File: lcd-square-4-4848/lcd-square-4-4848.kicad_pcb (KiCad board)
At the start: 2 copper layers, 77 x 77 mm, 42 parts, among them J1 SWD, J2 Conn_01x40_MountingPin, J4 USB_C_Receptacle_USB2.0_16P, SW1 BOOT0, SW2 RST, U1 siplex-som-s16, U2 TPS61169

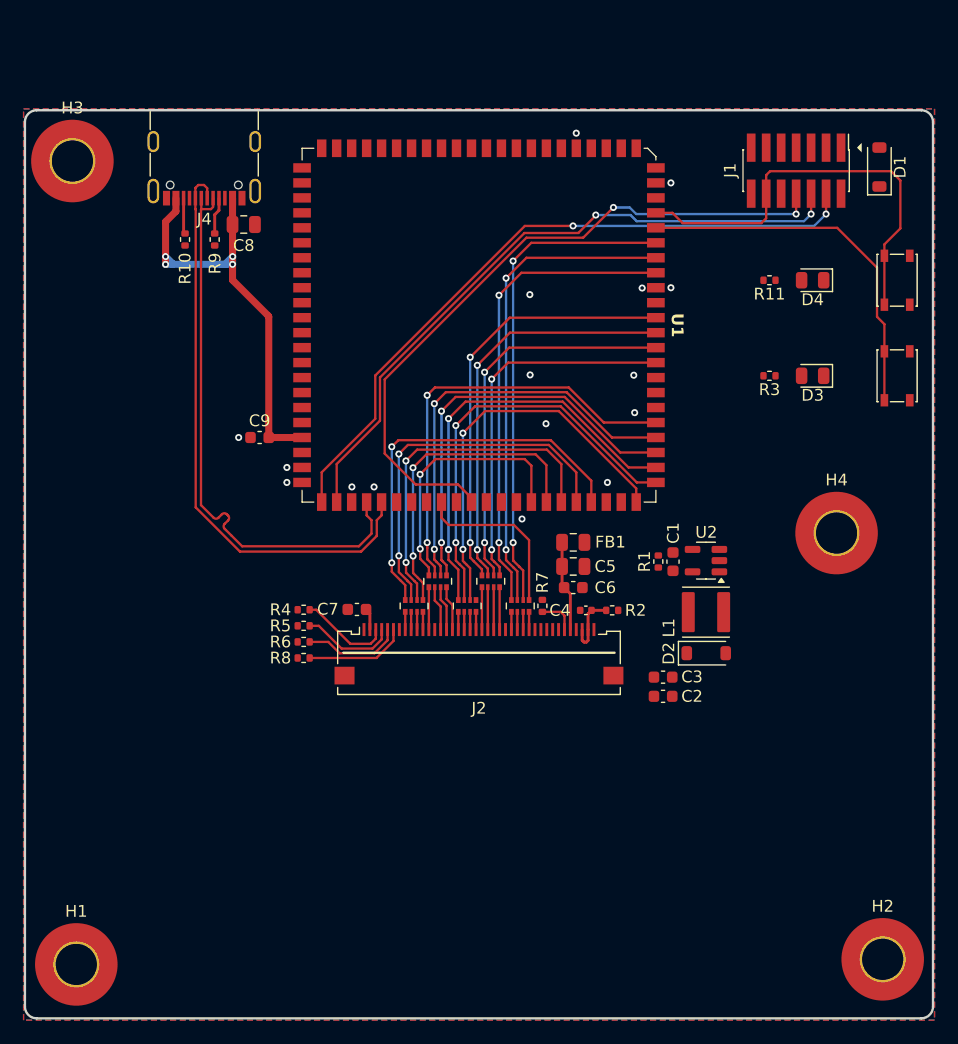
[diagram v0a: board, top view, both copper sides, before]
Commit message: LCD 4inch 480-480 on progress
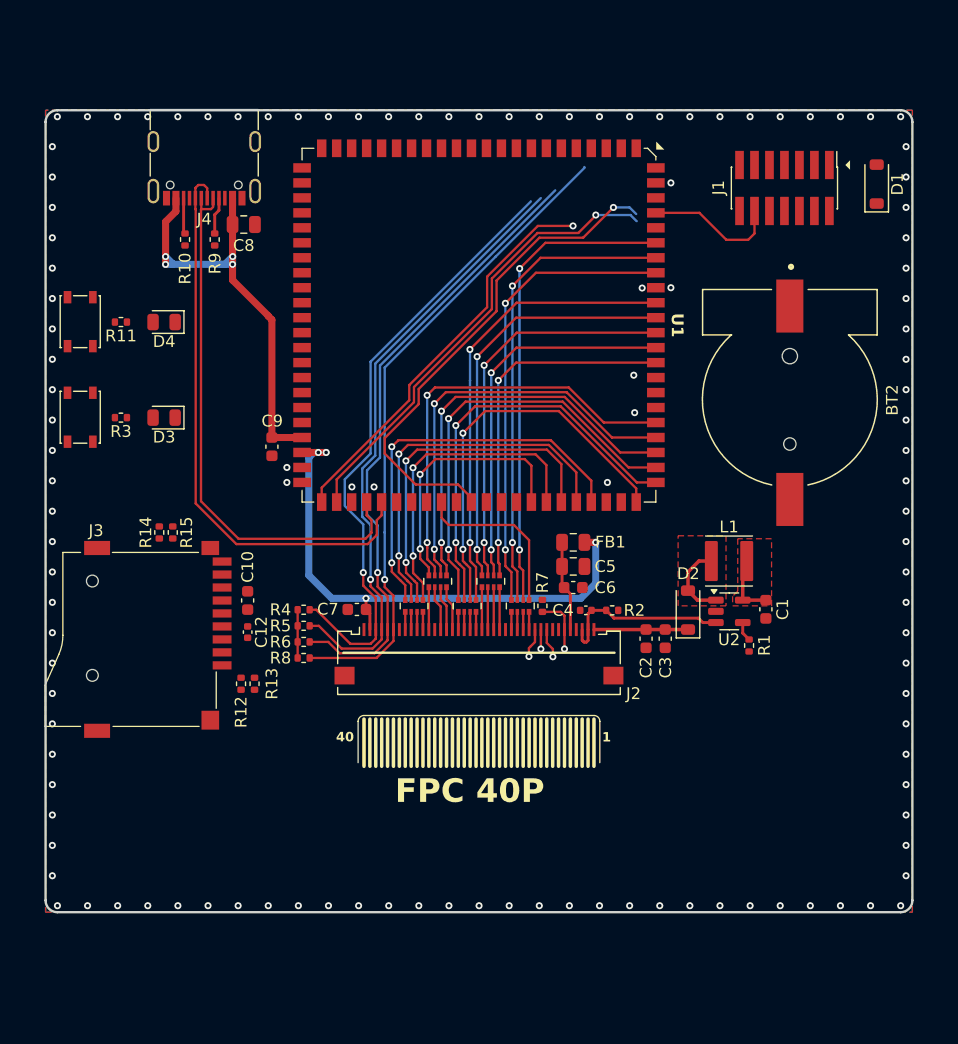
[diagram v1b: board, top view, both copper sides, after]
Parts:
- removed H1, H2, H3, H4: MountingHole_Pad, MountingHole:MountingHole_3.5mm_Pad_TopOnly
- added BT2: S8411-45R, CR1220-Batt-conn-S8411-45R:CR1220-Batt-conn-S8411-45R, F.Cu at (170.9, 83.5)
- added C10: 1u, Capacitor_SMD:C_0603_1608Metric, F.Cu at (124.9, 100.5)
- added C12: 100n, Capacitor_SMD:C_0402_1005Metric, F.Cu at (124.9, 103.1)
- added G***: LOGO, neochrom-logo:neochrom-logo-15, F.Cu at (168.3, 108.8)
- added J3: Micro_SD_Card_Det1, TF-115:SD-TF-115, F.Cu at (117.5, 103.8)
- added R12: 10K, Resistor_SMD:R_0402_1005Metric, F.Cu at (124.4, 107.5)
- added R13: 10K, Resistor_SMD:R_0402_1005Metric, F.Cu at (125.5, 107.5)
- added R14: 10K, Resistor_SMD:R_0402_1005Metric, F.Cu at (117.4, 94.7)
- added R15: 10K, Resistor_SMD:R_0402_1005Metric, F.Cu at (118.6, 94.7)
- moved SW1 69.4 mm to (110.7, 84.9)
- moved SW2 69.4 mm to (110.7, 76.8)
- moved D3 55.1 mm to (117.9, 85.0)
- moved D4 55.1 mm to (117.9, 76.9)
- moved R11 55.1 mm to (114.2, 76.9)
- moved R3 55.1 mm to (114.2, 85.0)
- moved R1 10.5 mm to (167.5, 104.3)
- moved C1 8.85 mm to (168.9, 101.2), turned to -90 degrees
- moved C2 5.10 mm to (158.7, 103.7), turned to -90 degrees
- moved L1 4.75 mm to (165.8, 97.1), turned to 180 degrees
- moved U2 4.74 mm to (165.8, 101.4), turned to 0 degrees
- moved D2 3.97 mm to (162.3, 101.3), turned to 90 degrees
- moved C3 3.27 mm to (160.4, 103.7), turned to -90 degrees
- moved J1 1.77 mm to (170.5, 65.5)
- moved D1 1.46 mm to (178.3, 65.2)
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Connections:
- net Net-(D2-A) renamed /SW
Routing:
- net +3V3: track 1.84 -> 50.7 mm, vias 0 -> 4
- net /LCD_TP_INT: track 8.67 -> 55.2 mm, vias 0 -> 1
- net /LCD_TP_SDA: track 8.36 -> 52.9 mm, vias 0 -> 1
- net /LCD_TP_RST: track 7.75 -> 51.7 mm, vias 0 -> 1
- net /LCD_TP_SCL: track 8.06 -> 51.6 mm, vias 0 -> 1
- net /B7: track 0.00 -> 38.9 mm, vias 0 -> 2
- net /BOOT0: track 31.7 -> 0.00 mm
- net /RESET: track 36.5 -> 11.4 mm
- net /SWDIO: track 58.2 -> 34.0 mm, vias 2 -> 1
- net /SWCLK: track 56.6 -> 39.2 mm, vias 2 -> 1
- net /SWO: track 58.4 -> 42.5 mm, vias 2 -> 1
- net /LED_K: track 5.45 -> 15.2 mm
- net /LED_A: track 0.00 -> 7.98 mm
- net /SW: track 0.00 -> 6.65 mm
- net +5V: track 0.00 -> 5.42 mm
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- added copper zone on F.Cu, net +5V
- added copper zone on F.Cu, net /SW
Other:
- board size 77 x 77 mm -> 73.5 x 68 mm
- board text added: "1"
- board text added: "40"
- board text added: "FPC 40P"
- board text removed: "FPC CONN EDGE"

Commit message: Change SD card orientation
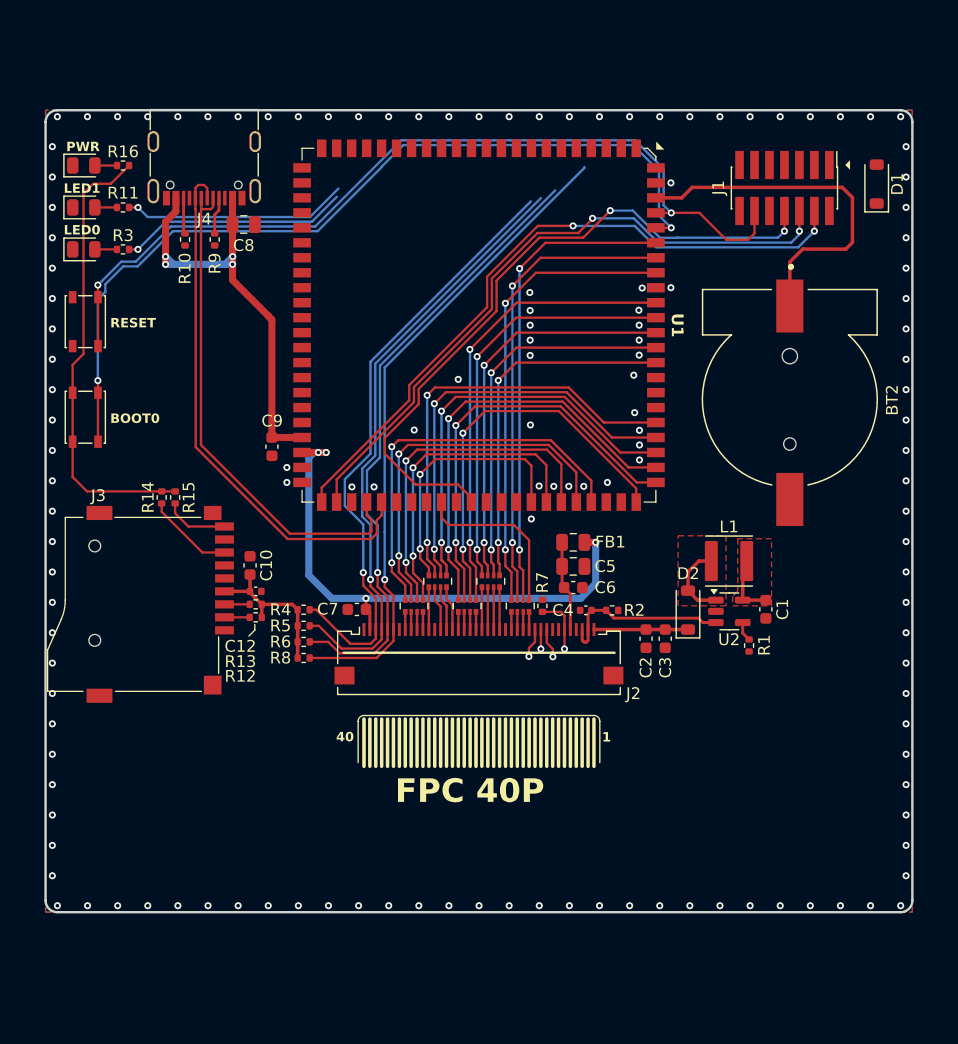
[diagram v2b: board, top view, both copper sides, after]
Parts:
- added D5: LED, LED_SMD:LED_0805_2012Metric, F.Cu at (111.0, 63.6)
- added R16: 2K, Resistor_SMD:R_0402_1005Metric, F.Cu at (114.4, 63.6)
- moved D3 15.8 mm to (111.0, 70.7), turned to 0 degrees
- moved R3 14.3 mm to (114.4, 70.7)
- moved D4 11.9 mm to (111.0, 67.1), turned to 0 degrees
- moved R11 9.72 mm to (114.4, 67.1)
- moved R13 6.73 mm to (125.6, 100.8), turned to 180 degrees
- moved R12 5.77 mm to (125.6, 101.9), turned to 180 degrees
- moved C12 3.52 mm to (125.6, 99.7), turned to 0 degrees
- moved J3 2.98 mm to (117.7, 100.8)
- moved R14 2.98 mm to (117.7, 91.7)
- moved R15 2.98 mm to (118.8, 91.7)
- moved C10 2.98 mm to (125.1, 97.5)
- moved SW1 0.43 mm to (111.2, 84.9), turned to -90 degrees
- moved SW2 0.43 mm to (111.2, 76.8), turned to -90 degrees
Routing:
- net /BOOT0: track 0.00 -> 72.9 mm, vias 0 -> 2
- net /RESET: track 11.4 -> 74.7 mm, vias 0 -> 2
- net +3V3: track 50.7 -> 98.6 mm
- net VBAT: track 0.00 -> 30.9 mm
- net /SWDIO: track 34.0 -> 57.5 mm, vias 1 -> 2
- net /LED0: track 0.00 -> 19.5 mm, vias 0 -> 1
- net /LED1: track 0.00 -> 19.1 mm, vias 0 -> 1
- net /SWCLK: track 39.2 -> 55.7 mm, vias 1 -> 2
- net /SWO: track 42.5 -> 57.6 mm, vias 1 -> 2
- net /DAT0: track 0.00 -> 7.46 mm
- net /SD_DET: track 0.00 -> 5.48 mm
- net /USB_DP: track 48.9 -> 45.7 mm
- net /USB_DN: track 46.3 -> 43.1 mm
- net /DAT3: track 0.00 -> 2.14 mm
- net /CMD: track 0.00 -> 2.14 mm
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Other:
- board text added: "BOOT0"
- board text added: "LED0"
- board text added: "LED1"
- board text added: "PWR"
- board text added: "RESET"

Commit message: Add standard 5inch and 7inch display both resistive and capacitive
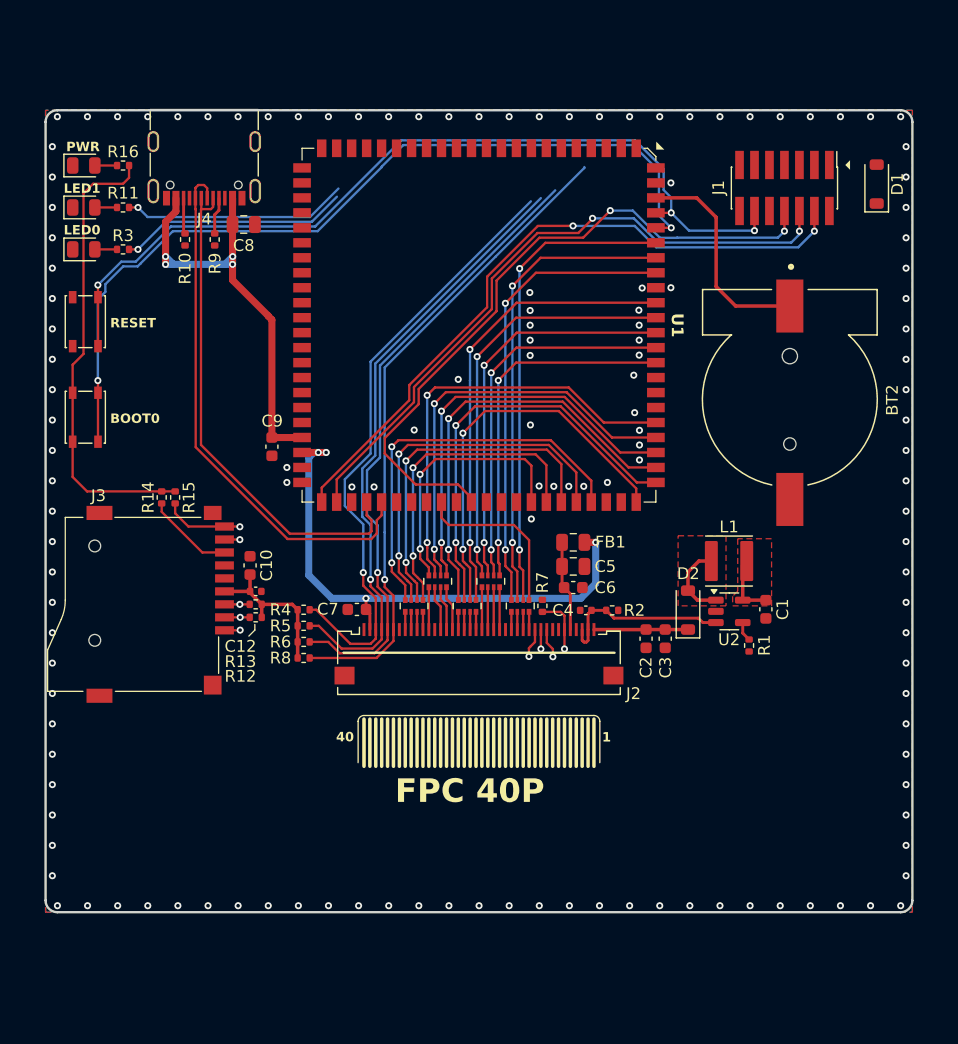
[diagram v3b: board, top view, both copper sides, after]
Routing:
- net VBAT: track 30.9 -> 18.6 mm
- net /DAT2: track 0.00 -> 1.34 mm, vias 0 -> 1
- net /SD_DET: track 5.48 -> 6.80 mm, vias 0 -> 1
- net /DAT1: track 0.00 -> 1.31 mm, vias 0 -> 1
- net /RESET: track 74.7 -> 73.9 mm, vias 2 -> 3
- net +3V3: track 98.6 -> 99.2 mm
- net /DAT3: vias 0 -> 1
- net /CMD: vias 0 -> 1

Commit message: LCD 4inch 480x480 98% finished, st-link left
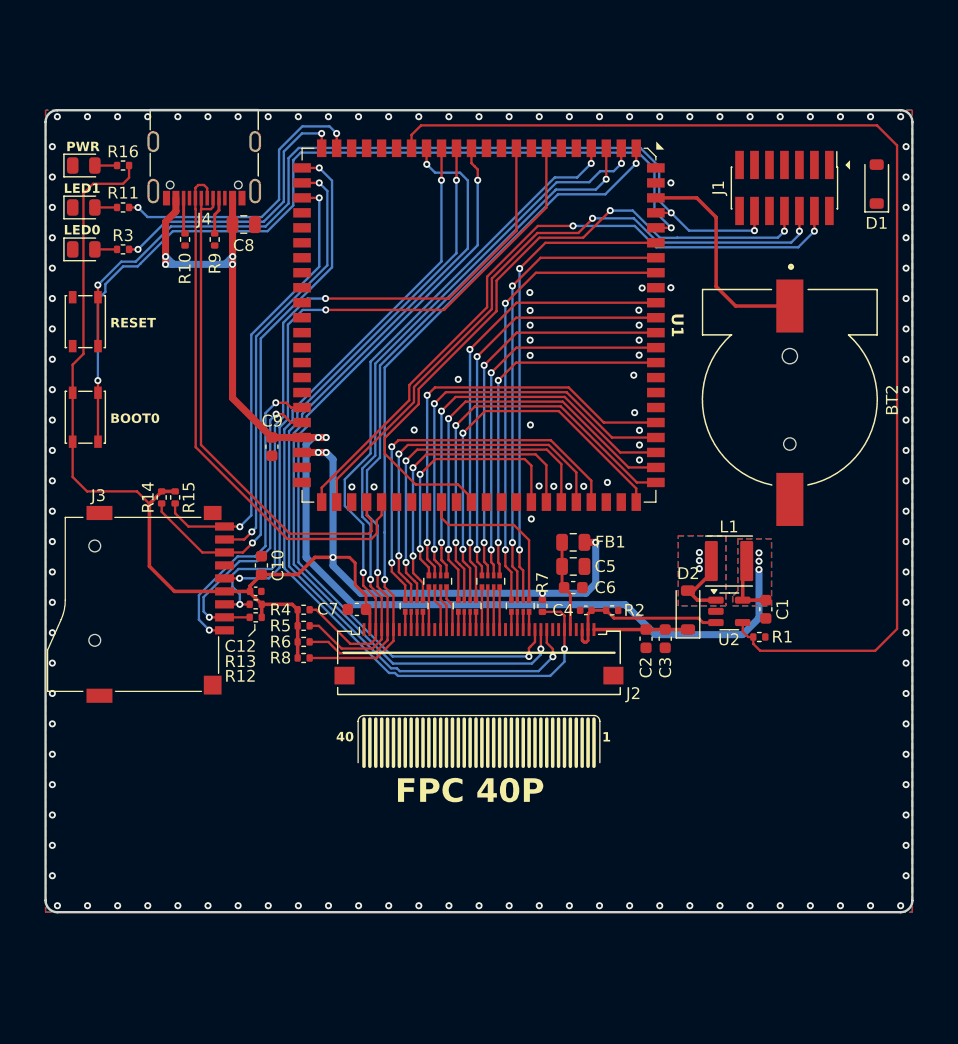
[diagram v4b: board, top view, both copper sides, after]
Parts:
- removed G***: LOGO, neochrom-logo:neochrom-logo-15
- moved R1 1.13 mm to (168.3, 103.6), turned to 0 degrees
- moved C10 0.97 mm to (126.1, 97.5)
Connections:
- C1 pad 1: +5V -> VBUS
- L1 pad 1: +5V -> VBUS
- R1 pad 1: +5V -> /LCD_BLK
- R1 pad 2: /LCD_BLK -> GND
- U1 pad 1: /LCD_RST -> /LCD_TP_INT
- U1 pad 12: unconnected-(U1-PA3-Pad12) -> /LCD_SPI_CS
- U1 pad 13: unconnected-(U1-PA7-Pad13) -> /LCD_SPI_DAT
- U1 pad 14: unconnected-(U1-PA6-Pad14) -> /LCD_RST
- U1 pad 15: unconnected-(U1-PA5-Pad15) -> /LCD_SPI_CLK
- U1 pad 16: unconnected-(U1-PB0-Pad16) -> /LCD_BLK
- U1 pad 21: unconnected-(U1-PB13-Pad21) -> /LED1
- U1 pad 22: unconnected-(U1-PB11-Pad22) -> /LED0
- U1 pad 23: unconnected-(U1-PB14-Pad23) -> /DAT0
- U1 pad 24: unconnected-(U1-PB15-Pad24) -> /DAT1
- U1 pad 25: unconnected-(U1-PH7-Pad25) -> /SD_DET
- U1 pad 39: /LCD_SPI_CLK -> /DAT2
- U1 pad 4: /LCD_TP_INT -> /LCD_TP_RST
- U1 pad 40: /LCD_SPI_CS -> /DAT3
- U1 pad 6: /LCD_TP_RST -> unconnected-(U1-PC0-Pad6)
- U1 pad 7: unconnected-(U1-PC1-Pad7) -> /CLK
- U1 pad 88: /LCD_SPI_DAT -> unconnected-(U1-PB5-Pad88)
- U1 pad 9: unconnected-(U1-PA0-Pad9) -> /CMD
- U2 pad 5: +5V -> VBUS
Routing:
- net /LCD_BLK: track 1.66 -> 100.0 mm
- net /LCD_RST: track 4.83 -> 75.1 mm, vias 1 -> 2
- net /LCD_SPI_CLK: track 1.65 -> 70.9 mm, vias 1 -> 2
- net /LCD_SPI_DAT: track 2.52 -> 70.4 mm, vias 1 -> 2
- net VBUS: track 39.3 -> 104.1 mm, vias 4 -> 9
- net /LCD_SPI_CS: track 2.49 -> 67.0 mm, vias 1 -> 2
- net /CMD: track 2.14 -> 59.7 mm, vias 1 -> 2
- net /CLK: track 0.00 -> 57.0 mm, vias 0 -> 2
- net /DAT0: track 7.46 -> 46.7 mm, vias 0 -> 2
- net /DAT1: track 1.31 -> 36.6 mm, vias 1 -> 2
- net /SD_DET: track 6.80 -> 38.9 mm, vias 1 -> 2
- net /DAT2: track 1.34 -> 26.9 mm, vias 1 -> 2
- net /DAT3: track 2.14 -> 26.8 mm, vias 1 -> 2
- net +3V3: track 99.2 -> 122.5 mm, vias 4 -> 5
- net /LCD_TP_SCL: track 51.6 -> 60.9 mm, vias 1 -> 2
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- added copper zone on B.Cu, net /SW
- added copper zone on B.Cu, net VBUS
- added copper zone on F.Cu, net VBUS
- removed copper zone on F.Cu, net +5V

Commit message: LCD 5inch, finished tracks, LCD square, Adding MAX98357A
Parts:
- added C11: 10u, Capacitor_SMD:C_0805_2012Metric, F.Cu at (119.9, 77.7)
- added J5: Conn_01x02_MountingPin, Connector_Hirose:Hirose_DF13C_CL535-0402-2-51_1x02-1MP_P1.25mm_Vertical, F.Cu at (112.4, 78.7)
- added R17: 100, Resistor_SMD:R_0402_1005Metric, F.Cu at (163.2, 53.7)
- added R18: 1M, Resistor_SMD:R_0402_1005Metric, F.Cu at (118.5, 85.9)
- added R19: 100K, Resistor_SMD:R_0402_1005Metric, F.Cu at (117.1, 85.9)
- added U3: siplex-som-s16, siplex:siplex-som-s16, F.Cu at (144.6, 77.1)
- U1: value siplex-som-s16 -> MAX98357A; footprint siplex:siplex-som-s16 -> Package_DFN_QFN:TQFN-16-1EP_3x3mm_P0.5mm_EP1.23x1.23mm
- moved SW1 69.2 mm to (177.0, 106.4), turned to 0 degrees
- moved SW2 64.9 mm to (168.9, 106.4), turned to 0 degrees
- moved U1 27.6 mm to (117.4, 81.9), turned to 90 degrees
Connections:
- J1 pad 11: unconnected-(J1-Pin_11-Pad11) -> Net-(J1-Pin_11)
- U1 pad 1: /LCD_TP_INT -> /I2S_SDO
- U1 pad 10: unconnected-(U1-PA1-Pad10) -> Net-(J5-Pin_2)
- U1 pad 11: unconnected-(U1-PA4-Pad11) -> GND
- U1 pad 12: /LCD_SPI_CS -> unconnected-(U1-NC-Pad12)
- U1 pad 13: /LCD_SPI_DAT -> unconnected-(U1-NC-Pad13)
- U1 pad 14: /LCD_RST -> /I2S_WS
- U1 pad 15: /LCD_SPI_CLK -> GND
- U1 pad 16: /LCD_BLK -> /I2S_SCLK
- U1 pad 17: unconnected-(U1-PB1-Pad17) -> GND
- U1 pad 2: /LCD_TP_SCL -> Net-(U1-GAIN_SLOT)
- U1 pad 3: /LCD_TP_SDA -> GND
- U1 pad 4: /LCD_TP_RST -> Net-(U1-~{SD_MODE})
- U1 pad 5: GND -> unconnected-(U1-NC-Pad5)
- U1 pad 7: /CLK -> VBUS
- U1 pad 8: unconnected-(U1-PC4-Pad8) -> VBUS
- U1 pad 9: /CMD -> Net-(J5-Pin_1)
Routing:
- net Net-(RN4-R4.2): track 14.6 -> 37.0 mm
- net /RESET: track 75.5 -> 62.2 mm
- net /BOOT0: track 74.5 -> 62.6 mm
- net /I2S_SCLK: track 0.00 -> 10.5 mm, vias 0 -> 1
- net /I2S_SDO: track 0.00 -> 7.25 mm, vias 0 -> 1
- net Net-(J5-Pin_1): track 0.00 -> 6.53 mm
- net +3V3: track 122.5 -> 127.3 mm
- net VBUS: track 104.1 -> 108.7 mm
- net Net-(J5-Pin_2): track 0.00 -> 4.50 mm
- net /R4: track 26.9 -> 23.1 mm
- net /R3: track 22.2 -> 18.4 mm
- net /R5: track 29.5 -> 26.4 mm
- net /R6: track 31.7 -> 29.0 mm
- net Net-(RN4-R1.2): track 39.2 -> 41.5 mm
- net /R7: track 33.9 -> 31.6 mm
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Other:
- board text removed: "BOOT0"
- board text removed: "RESET"
